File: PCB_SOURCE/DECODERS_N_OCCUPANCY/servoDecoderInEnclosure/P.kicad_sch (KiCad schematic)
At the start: 7 parts, among them J601 Conn_01x03_Pin, Q801 AO3400A

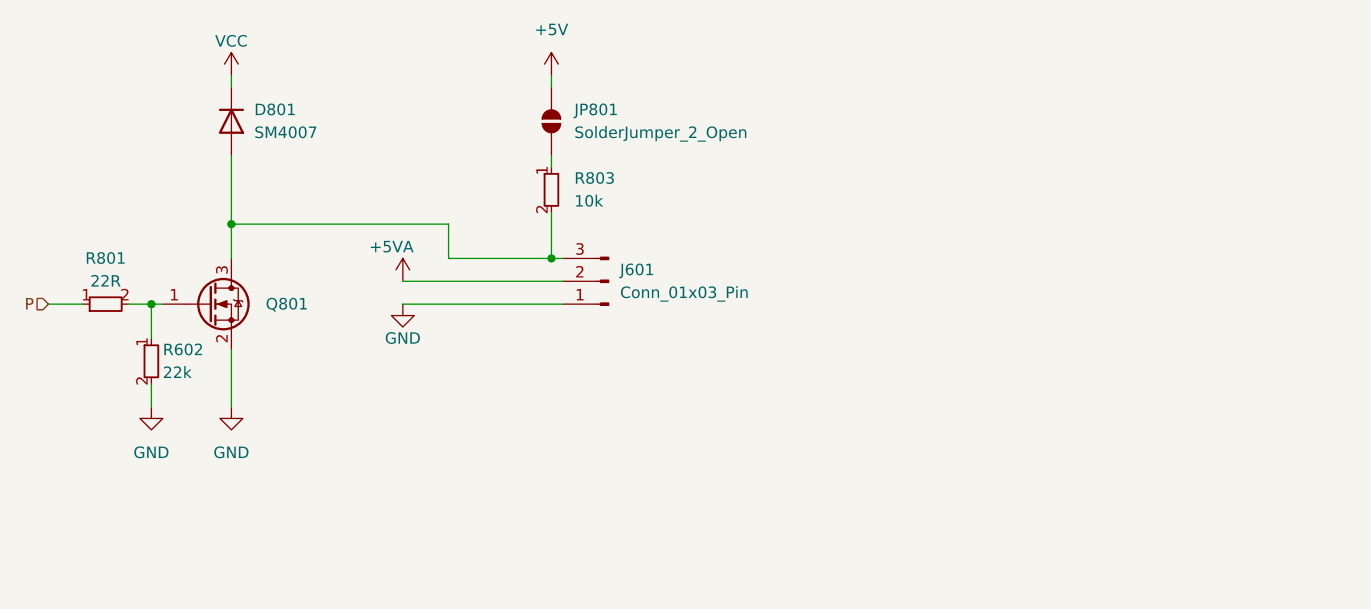
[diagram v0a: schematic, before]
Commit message: added S88 current sense to releases and update OSSD decoder
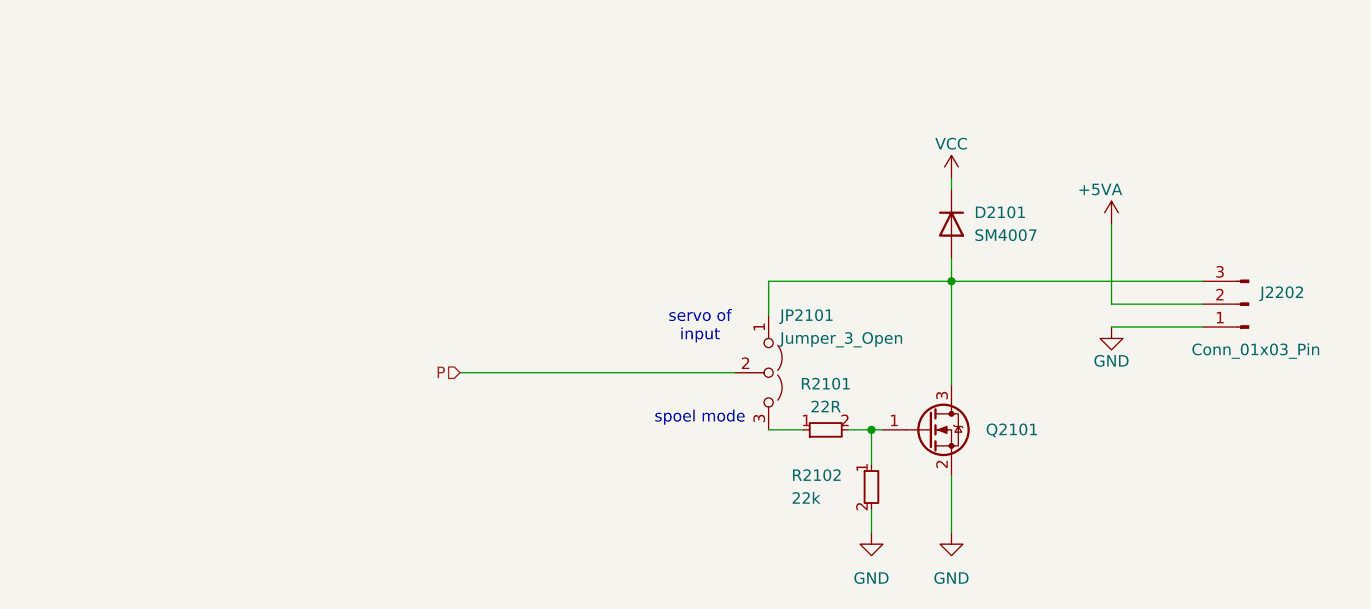
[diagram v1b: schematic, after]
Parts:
- removed JP801: SolderJumper_2_Open, Jumper:SolderJumper-2_P1.3mm_Open_RoundedPad1.0x1.5mm, symbol Jumper:SolderJumper_2_Open
- removed R602: 22k, custom_kicad_lib_sk:R_0603_smalltext, symbol resistors_0603:R_22k_0603
- removed R801: 22R, custom_kicad_lib_sk:R_0603_smalltext, symbol resistors_0603:R_22R_0603
- removed R803: 10k, custom_kicad_lib_sk:R_0603_smalltext, symbol resistors_0603:R_10k_0603
- added JP2101: Jumper_3_Open, Jumper:SolderJumper-3_P1.3mm_Open_RoundedPad1.0x1.5mm, symbol Jumper:Jumper_3_Open
- added R2101: 22R, custom_kicad_lib_sk:R_0603_smalltext, symbol resistors_0603:R_22R_0603
- added R2102: 22k, custom_kicad_lib_sk:R_0603_smalltext, symbol resistors_0603:R_22k_0603
- renumbered D801 to D2101, J601 to J2202, Q801 to Q2101
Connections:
- net GND: now also R2102.2
- net P: now also JP2101.2 (C)
- net at D2101.2 (A), J2202.3 (Pin_3), Q2101.3 (D): now also JP2101.1 (A)
- net at Q2101.1 (G): now also R2101.2, R2102.1
- new net: JP2101.3 (B), R2101.1
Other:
- note added: "servo of input"
- note added: "spoel mode"
- moved on the sheet: D2101, J2202, Q2101

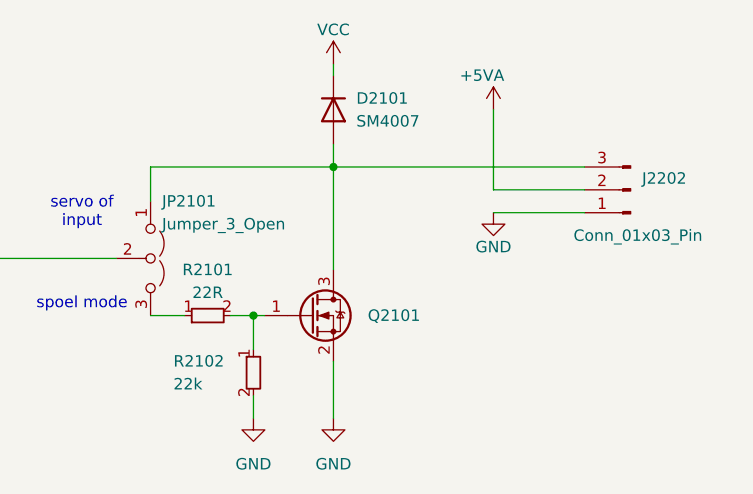
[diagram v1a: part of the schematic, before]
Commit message: upgraded servo driver code to newest standard
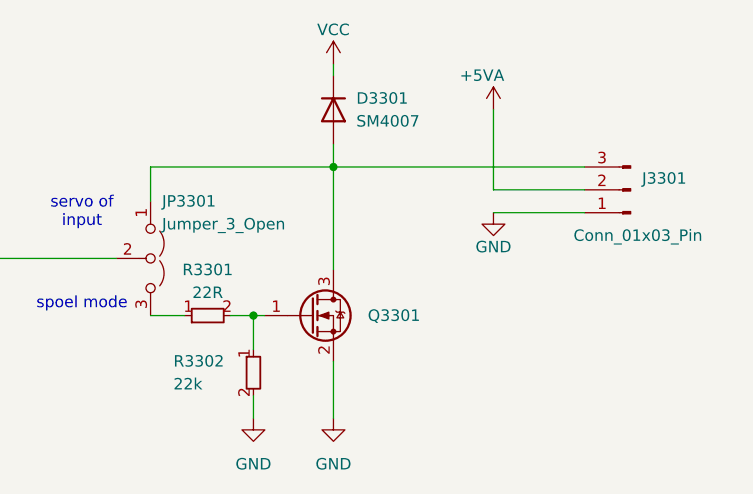
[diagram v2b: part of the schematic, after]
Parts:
- renumbered D2101 to D3301, J2202 to J3301, JP2101 to JP3301, Q2101 to Q3301, R2101 to R3301, R2102 to R3302
